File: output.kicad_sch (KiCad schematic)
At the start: 31 parts, among them J2 SMA, J3 SMA, J4 SMA, J5 U.Fl, T2 MABA-010247-2R1250, U31 TLV3601DCKR, U32 TLV3601DCKR

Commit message: DRC clean-up.
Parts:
- renumbered C37 to C3
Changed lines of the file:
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@@
 		(on_board yes)
 		(dnp no)
-		(property "Reference" "C37"
+		(property "Reference" "C3"
 			(at 70.866 103.886 90)
 			(effects
@@
 			(project "gpsref"
 				(path "/3160ff17-81c2-4674-af97-e8d9acaf6b65/26994282-45a2-461a-b033-dde2ded4d8ff"
-					(reference "C37")
+					(reference "C3")
 					(unit 1)
 				)

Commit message: Route extint.
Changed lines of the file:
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@@
 	(generator_version "9.0")
 	(paper "A4")
-	(text_box "Eyeballing the datasheet, the TLV3601 output resistance is in the ballpark of 50ohm."
+	(text_box "Eyeballing the datasheet, the TLV3601 output resistance is in the ballpark of 50Ω."
 		(exclude_from_sim no)
 		(at 90.5881 98.8639 0)

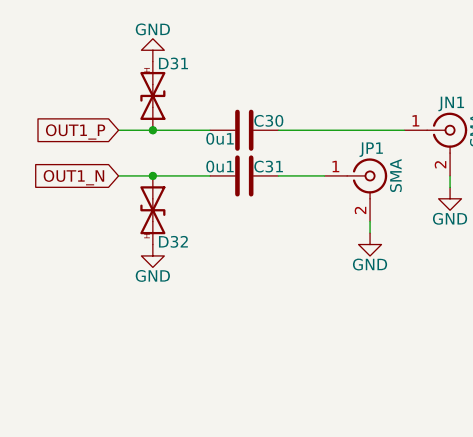
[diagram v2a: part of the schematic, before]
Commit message: Nix a DRC error.
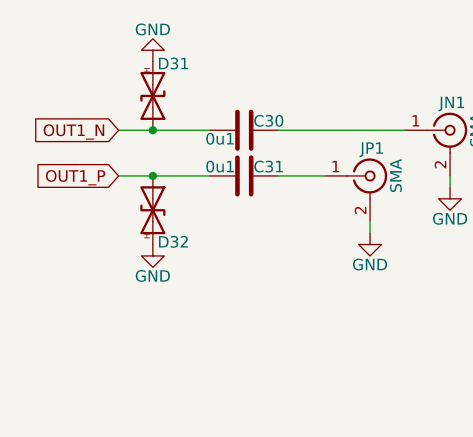
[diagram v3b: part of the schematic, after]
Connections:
- net OUT1_N: now also C30.1, D31.1 (A1); no longer C31.1, D32.1 (A1)
- net OUT1_P: now also C31.1, D32.1 (A1); no longer C30.1, D31.1 (A1)
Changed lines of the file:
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@@
 	(global_label "OUT1_N"
 		(shape input)
-		(at 50.8 67.31 180)
+		(at 50.8 62.23 180)
 		(fields_autoplaced yes)
 		(effects
@@
 		)
 		(property "Intersheetrefs" "${INTERSHEET_REFS}"
-			(at 40.6786 67.31 0)
+			(at 40.7391 62.23 0)
 			(effects
 				(font
@@
 	(global_label "OUT1_P"
 		(shape input)
-		(at 50.8 62.23 180)
+		(at 50.8 67.31 180)
 		(fields_autoplaced yes)
 		(effects
@@
 		)
 		(property "Intersheetrefs" "${INTERSHEET_REFS}"
-			(at 40.7391 62.23 0)
+			(at 40.6786 67.31 0)
 			(effects
 				(font

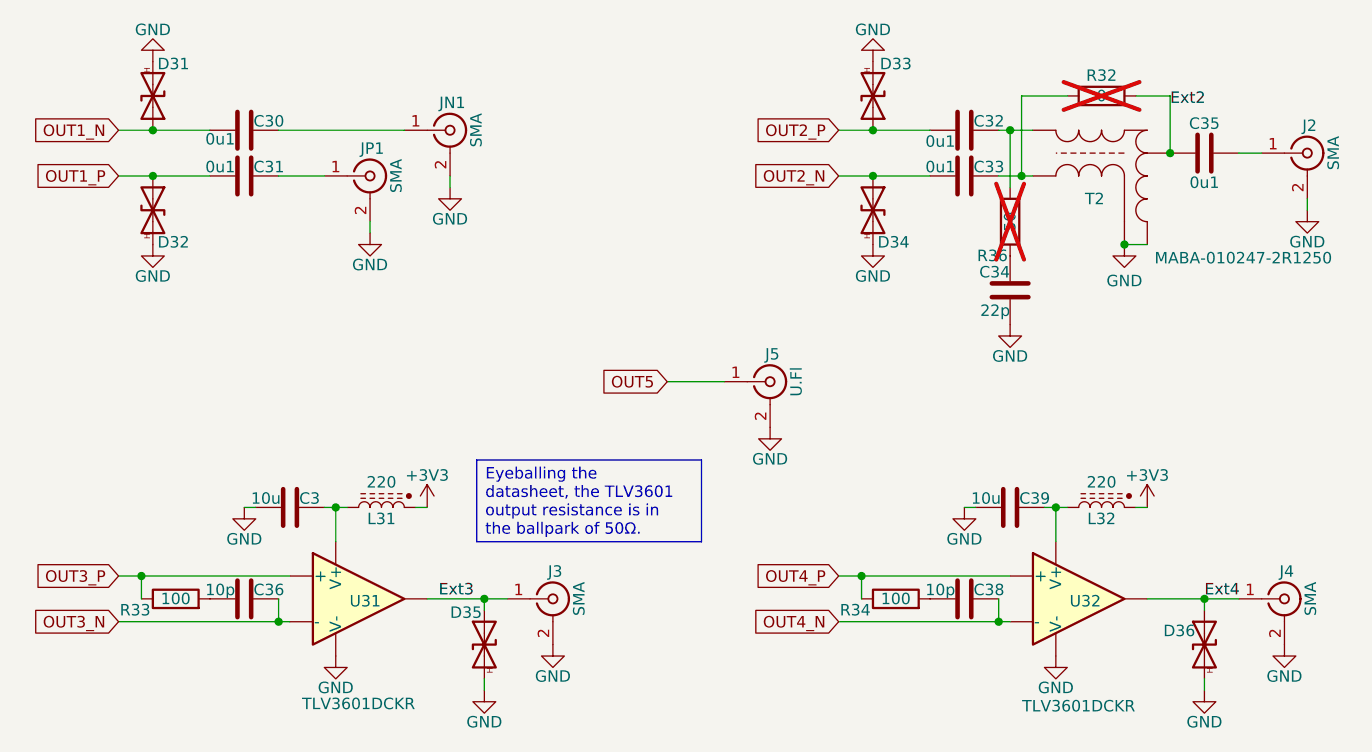
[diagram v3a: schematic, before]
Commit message: Add bias resistors to comparators.
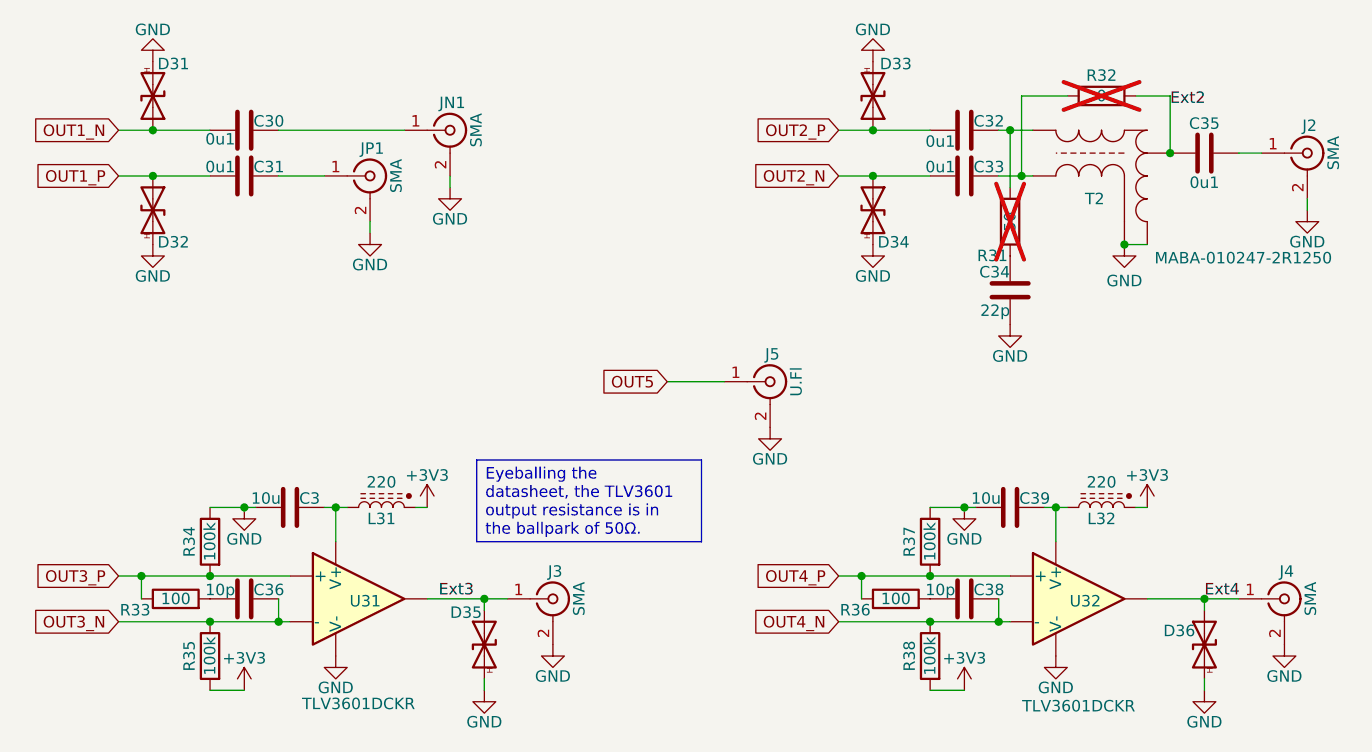
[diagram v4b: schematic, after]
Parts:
- added R34, R35, R37, R38: 100k, Resistor_SMD:R_0402_1005Metric, symbol Device:R
- renumbered R36 to R31, R34 to R36
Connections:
- net +3V3: now also R35.2, R38.2
- net GND: now also R34.1, R37.1
- net OUT3_N: now also R35.1
- net OUT3_P: now also R34.2
- net OUT4_N: now also R38.1
- net OUT4_P: now also R37.2

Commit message: Simplify CMOS output structure.
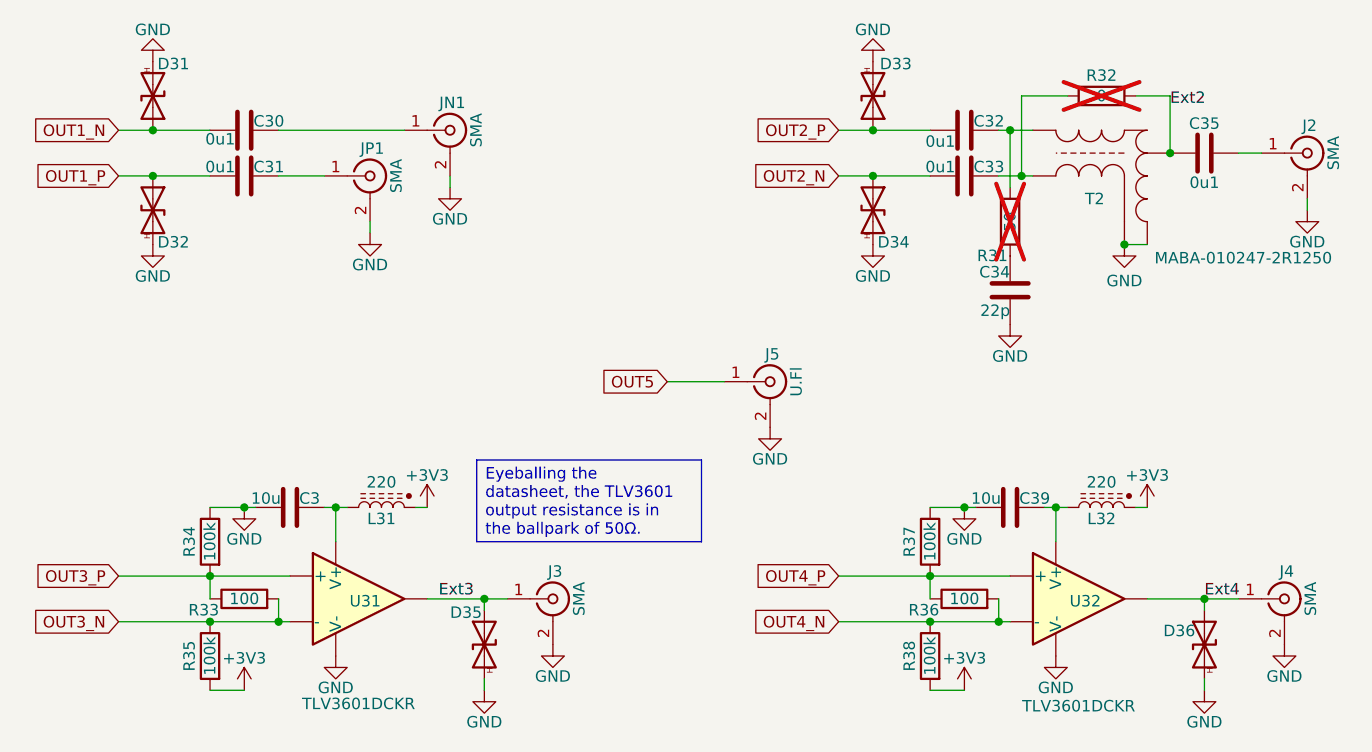
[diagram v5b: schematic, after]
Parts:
- removed C36, C38: 10p, Capacitor_SMD:C_0402_1005Metric, symbol Device:C
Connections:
- net OUT3_N: now also R33.2
- net OUT4_N: now also R36.2
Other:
- moved on the sheet: R33, R36
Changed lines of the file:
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@@
 	)
 	(junction
-		(at 53.34 111.76)
-		(diameter 0)
-		(color 0 0 0 0)
-	)
-	(junction
 		(at 151.13 67.31)
 		(diameter 0)
@@
 	)
 	(junction
-		(at 133.35 111.76)
-		(diameter 0)
-		(color 0 0 0 0)
-	)
-	(junction
 		(at 68.58 116.84)
 		(diameter 0)
@@
 	(wire
 		(pts
-			(xy 50.8 111.76) (xy 53.34 111.76)
+			(xy 50.8 111.76) (xy 60.96 111.76)
 		)
 		(stroke
@@
 	(wire
 		(pts
-			(xy 53.34 111.76) (xy 53.34 114.3)
+			(xy 60.96 111.76) (xy 60.96 114.3)
 		)
 		(stroke
@@
 	(wire
 		(pts
-			(xy 130.81 111.76) (xy 133.35 111.76)
+			(xy 130.81 111.76) (xy 140.97 111.76)
 		)
 		(stroke
@@
 	(wire
 		(pts
-			(xy 133.35 111.76) (xy 140.97 111.76)
-		)
-		(stroke
-			(width 0)
-			(type default)
-		)
-	)
-	(wire
-		(pts
 			(xy 151.13 58.42) (xy 156.21 58.42)
 		)
@@
 	(wire
 		(pts
-			(xy 53.34 111.76) (xy 60.96 111.76)
-		)
-		(stroke
-			(width 0)
-			(type default)
-		)
-	)
-	(wire
-		(pts
 			(xy 167.64 58.42) (xy 167.64 64.77)
 		)
@@
 	(wire
 		(pts
-			(xy 133.35 111.76) (xy 133.35 114.3)
+			(xy 140.97 111.76) (xy 140.97 114.3)
 		)
 		(stroke
@@
 	(symbol
 		(lib_id "Device:R")
-		(at 57.15 114.3 90)
+		(at 64.77 114.3 90)
 		(unit 1)
 		(exclude_from_sim no)
@@
 		(dnp no)
 		(property "Reference" "R33"
-			(at 54.356 114.808 90)
+			(at 61.976 114.808 90)
 			(effects
 				(font
@@
 		)
 		(property "Value" "100"
-			(at 57.15 114.3 90)
+			(at 64.77 114.3 90)
 			(effects
 				(font
@@
 		)
 		(property "Footprint" "Resistor_SMD:R_0402_1005Metric"
-			(at 57.15 116.078 90)
+			(at 64.77 116.078 90)
 			(effects
 				(font
@@
 		)
 		(property "Datasheet" "~"
-			(at 57.15 114.3 0)
+			(at 64.77 114.3 0)
 			(effects
 				(font
@@
 		)
 		(property "Description" "Resistor"
-			(at 57.15 114.3 0)
+			(at 64.77 114.3 0)
 			(effects
 				(font
@@
 		)
 		(property "LCSC" "C25076"
-			(at 57.15 114.3 90)
+			(at 64.77 114.3 90)
 			(effects
 				(font
@@
 	(symbol
 		(lib_id "Device:C")
-		(at 144.78 114.3 90)
-		(unit 1)
-		(exclude_from_sim no)
-		(in_bom yes)
-		(on_board yes)
-		(dnp no)
-		(property "Reference" "C38"
-			(at 145.796 114.046 90)
-			(effects
-				(font
-					(size 1.27 1.27)
-				)
-				(justify right top)
-			)
-		)
-		(property "Value" "10p"
-			(at 143.764 114.046 90)
-			(effects
-				(font
-					(size 1.27 1.27)
-				)
-				(justify left top)
-			)
-		)
-		(property "Footprint" "Capacitor_SMD:C_0402_1005Metric"
-			(at 148.59 113.3348 0)
-			(effects
-				(font
-					(size 1.27 1.27)
-				)
-				(hide yes)
-			)
-		)
-		(property "Datasheet" "~"
-			(at 144.78 114.3 0)
-			(effects
-				(font
-					(size 1.27 1.27)
-				)
-				(hide yes)
-			)
-		)
-		(property "Description" "Unpolarized capacitor"
-			(at 144.78 114.3 0)
-			(effects
-				(font
-					(size 1.27 1.27)
-				)
-				(hide yes)
-			)
-		)
-		(property "LCSC" "C32949"
-			(at 144.78 114.3 90)
-			(effects
-				(font
-					(size 1.27 1.27)
-				)
-				(hide yes)
-			)
-		)
-		(pin "1"
-		)
-		(pin "2"
-		)
-		(instances
-			(project "gpsref"
-				(path "/3160ff17-81c2-4674-af97-e8d9acaf6b65/26994282-45a2-461a-b033-dde2ded4d8ff"
-					(reference "C38")
-					(unit 1)
-				)
-			)
-		)
-	)
-	(symbol
-		(lib_id "Device:C")
 		(at 64.77 62.23 90)
 		(unit 1)
@@
 	(symbol
 		(lib_id "Device:R")
-		(at 137.16 114.3 90)
+		(at 144.78 114.3 90)
 		(unit 1)
 		(exclude_from_sim no)
@@
 		(dnp no)
 		(property "Reference" "R36"
-			(at 134.366 114.808 90)
+			(at 141.986 114.808 90)
 			(effects
 				(font
@@
 		)
 		(property "Value" "100"
-			(at 137.16 114.3 90)
+			(at 144.78 114.3 90)
 			(effects
 				(font
@@
 		)
 		(property "Footprint" "Resistor_SMD:R_0402_1005Metric"
-			(at 137.16 116.078 90)
+			(at 144.78 116.078 90)
 			(effects
 				(font
@@
 		)
 		(property "Datasheet" "~"
-			(at 137.16 114.3 0)
+			(at 144.78 114.3 0)
 			(effects
 				(font
@@
 		)
 		(property "Description" "Resistor"
-			(at 137.16 114.3 0)
+			(at 144.78 114.3 0)
 			(effects
 				(font
@@
 		)
 		(property "LCSC" "C25076"
-			(at 137.16 114.3 90)
+			(at 144.78 114.3 90)
 			(effects
 				(font
@@
 					(unit 1)
 				)
-			)
-		)
-	)
-	(symbol
-		(lib_id "Device:C")
-		(at 64.77 114.3 90)
-		(unit 1)
-		(exclude_from_sim no)
-		(in_bom yes)
-		(on_board yes)
-		(dnp no)
-		(property "Reference" "C36"
-			(at 65.786 114.046 90)
-			(effects
-				(font
-					(size 1.27 1.27)
-				)
-				(justify right top)
-			)
-		)
-		(property "Value" "10p"
-			(at 63.754 114.046 90)
-			(effects
-				(font
-					(size 1.27 1.27)
-				)
-				(justify left top)
-			)
-		)
-		(property "Footprint" "Capacitor_SMD:C_0402_1005Metric"
-			(at 68.58 113.3348 0)
-			(effects
-				(font
-					(size 1.27 1.27)
-				)
-				(hide yes)
-			)
-		)
-		(property "Datasheet" "~"
-			(at 64.77 114.3 0)
-			(effects
-				(font
-					(size 1.27 1.27)
-				)
-				(hide yes)
-			)
-		)
-		(property "Description" "Unpolarized capacitor"
-			(at 64.77 114.3 0)
-			(effects
-				(font
-					(size 1.27 1.27)
-				)
-				(hide yes)
-			)
-		)
-		(property "LCSC" "C32949"
-			(at 64.77 114.3 90)
-			(effects
-				(font
-					(size 1.27 1.27)
-				)
-				(hide yes)
-			)
-		)
-		(pin "1"
-		)
-		(pin "2"
-		)
-		(instances
-			(project "gpsref"
-				(path "/3160ff17-81c2-4674-af97-e8d9acaf6b65/26994282-45a2-461a-b033-dde2ded4d8ff"
-					(reference "C36")
-					(unit 1)
-				)
